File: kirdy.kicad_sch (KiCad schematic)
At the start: 10 parts, among them J1 Kirdy Front Panel, J12 Kirdy LD Adapter

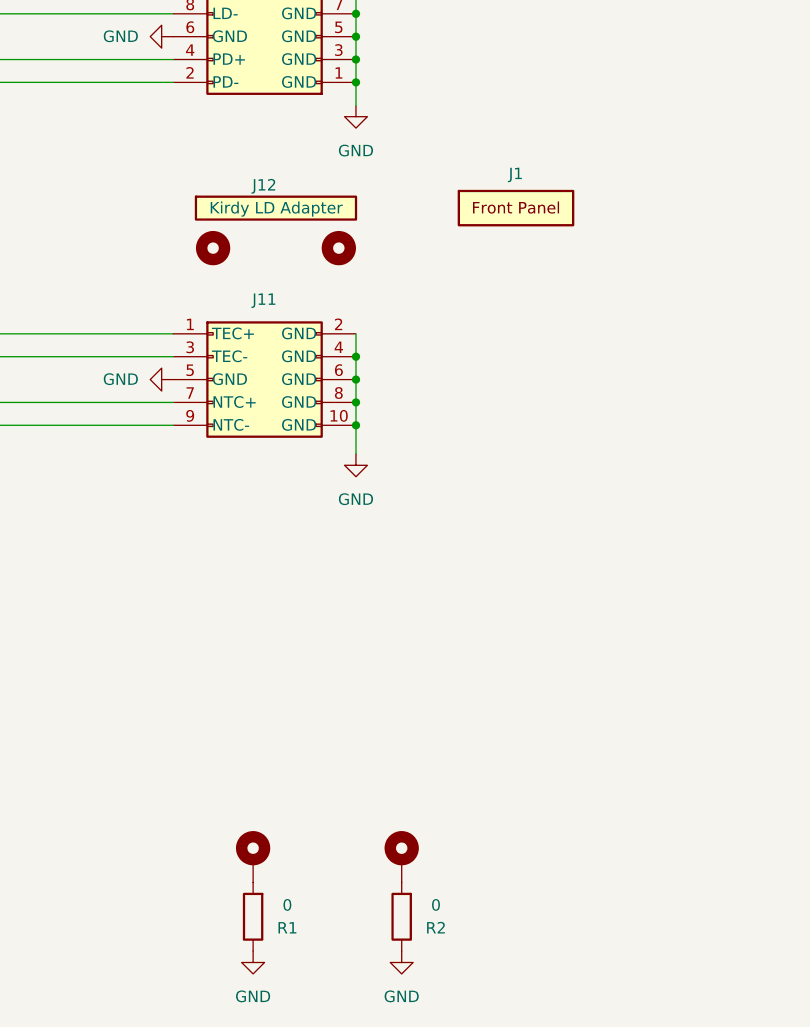
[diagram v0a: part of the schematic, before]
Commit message: sch, pcb:Edit PCB shape for connectors to protrude - Connectors now protrude the front panel - Align the connectors by the outline generated from 3D Model - Update the front panel symbol to include the two mounting holes
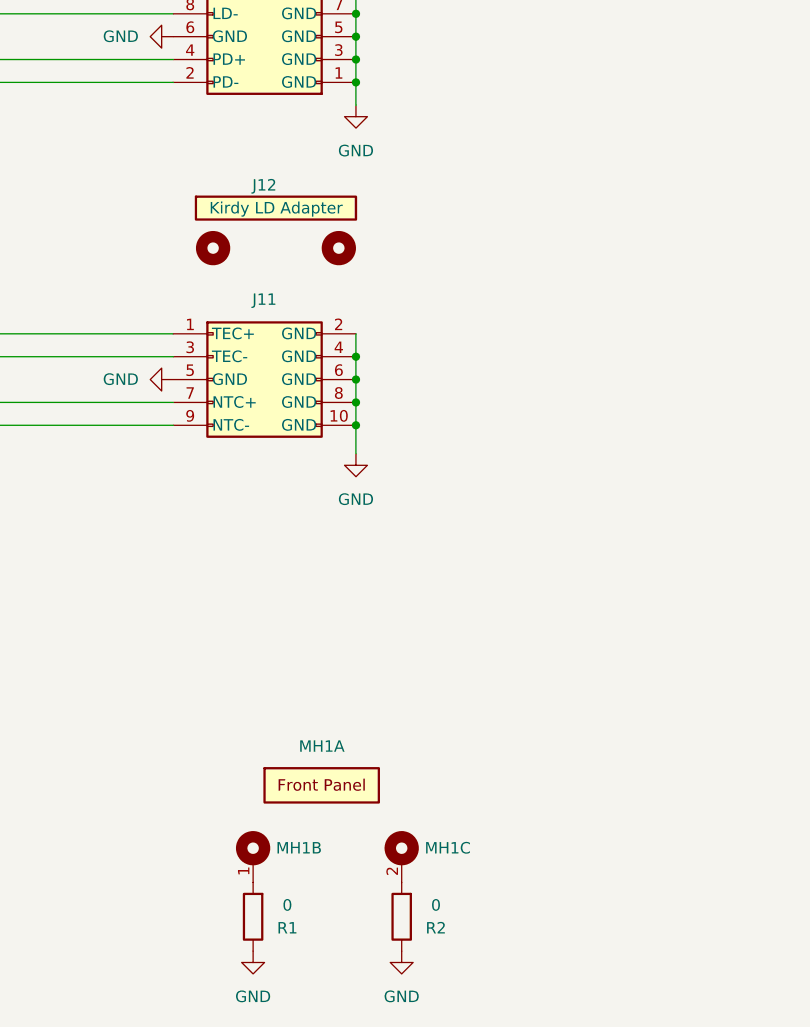
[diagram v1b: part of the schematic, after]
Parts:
- removed H1, H2: MountingHole_Pad, MountingHole:MountingHole_2.7mm_M2.5_Pad_Via, symbol Mechanical:MountingHole_Pad
- added unit 3 of MH1
- added unit 2 of MH1
- renumbered J1 to MH1
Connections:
- net at R1.2: now also MH1.1
- net at R2.2: now also MH1.2
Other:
- moved on the sheet: MH1A
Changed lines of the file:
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@@
+    )
+  )
+  (symbol (lib_id "kirdy:Panel") (at 309.88 208.28 270) (unit 3)
+    (in_bom yes) (on_board yes) (dnp no) (fields_autoplaced)
+    (property "Reference" "MH1" (at 312.42 208.28 90)
+      (effects (font (size 1.27 1.27)) (justify left))
+    )
+    (property "Value" "Kirdy Front Panel" (at 309.88 208.28 0)
+      (effects (font (size 1.27 1.27)) hide)
+    )
+    (property "Footprint" "kirdy:Panel" (at 309.88 208.28 0)
+      (effects (font (size 1.27 1.27)) hide)
+    )
+    (property "Datasheet" "" (at 309.88 208.28 0)
+      (effects (font (size 1.27 1.27)) hide)
+    )
+    (property "MFR_PN" "Kirdy Front Panel" (at 309.88 208.28 0)
+      (effects (font (size 1.27 1.27)) hide)
+    )
+    (pin "1")
+    (pin "2")
+    (instances
+      (project "kirdy"
+        (path "/88da1dd8-9274-4b55-84fb-90006c9b6e8f"
+          (reference "MH1") (unit 3)
+        )
+      )
     )
   )
@@
     )
   )
-  (symbol (lib_id "kirdy:Panel") (at 316.23 135.255 0) (unit 1)
-    (in_bom yes) (on_board yes) (dnp no) (fields_autoplaced)
-    (property "Reference" "J1" (at 322.58 133.35 0)
-      (effects (font (size 1.27 1.27)))
-    )
-    (property "Value" "Kirdy Front Panel" (at 316.23 135.255 0)
-      (effects (font (size 1.27 1.27)) hide)
-    )
-    (property "Footprint" "kirdy:Panel" (at 316.23 135.255 0)
-      (effects (font (size 1.27 1.27)) hide)
-    )
-    (property "Datasheet" "" (at 316.23 135.255 0)
-      (effects (font (size 1.27 1.27)) hide)
-    )
-    (property "MFR_PN" "Kirdy Front Panel" (at 322.58 133.35 0)
-      (effects (font (size 1.27 1.27)) hide)
-    )
-    (instances
-      (project "kirdy"
-        (path "/88da1dd8-9274-4b55-84fb-90006c9b6e8f"
-          (reference "J1") (unit 1)
+  (symbol (lib_name "Panel_1") (lib_id "kirdy:Panel") (at 294.64 199.39 0) (unit 1)
+    (in_bom yes) (on_board yes) (dnp no) (fields_autoplaced)
+    (property "Reference" "MH1" (at 300.99 196.977 0)
+      (effects (font (size 1.27 1.27)))
+    )
+    (property "Value" "Kirdy Front Panel" (at 294.64 199.39 0)
+      (effects (font (size 1.27 1.27)) hide)
+    )
+    (property "Footprint" "kirdy:Panel" (at 294.64 199.39 0)
+      (effects (font (size 1.27 1.27)) hide)
+    )
+    (property "Datasheet" "" (at 294.64 199.39 0)
+      (effects (font (size 1.27 1.27)) hide)
+    )
+    (property "MFR_PN" "Kirdy Front Panel" (at 300.99 197.485 0)
+      (effects (font (size 1.27 1.27)) hide)
+    )
+    (pin "1")
+    (pin "2")
+    (instances
+      (project "kirdy"
+        (path "/88da1dd8-9274-4b55-84fb-90006c9b6e8f"
+          (reference "MH1") (unit 1)
         )
       )
@@
     )
   )
-  (symbol (lib_id "Mechanical:MountingHole_Pad") (at 293.37 209.55 0) (unit 1)
-    (in_bom no) (on_board yes) (dnp no) (fields_autoplaced)
-    (property "Reference" "H1" (at 295.91 207.0099 0)
-      (effects (font (size 1.27 1.27)) (justify left) hide)
-    )
-    (property "Value" "MountingHole_Pad" (at 295.91 209.5499 0)
-      (effects (font (size 1.27 1.27)) (justify left) hide)
-    )
-    (property "Footprint" "MountingHole:MountingHole_2.7mm_M2.5_Pad_Via" (at 293.37 209.55 0)
-      (effects (font (size 1.27 1.27)) hide)
-    )
-    (property "Datasheet" "~" (at 293.37 209.55 0)
-      (effects (font (size 1.27 1.27)) hide)
-    )
-    (pin "1")
-    (instances
-      (project "kirdy"
-        (path "/88da1dd8-9274-4b55-84fb-90006c9b6e8f"
-          (reference "H1") (unit 1)
-        )
-      )
-    )
-  )
-  (symbol (lib_id "Mechanical:MountingHole_Pad") (at 309.88 209.55 0) (unit 1)
-    (in_bom no) (on_board yes) (dnp no) (fields_autoplaced)
-    (property "Reference" "H2" (at 312.42 207.0099 0)
-      (effects (font (size 1.27 1.27)) (justify left) hide)
-    )
-    (property "Value" "MountingHole_Pad" (at 312.42 209.5499 0)
-      (effects (font (size 1.27 1.27)) (justify left) hide)
-    )
-    (property "Footprint" "MountingHole:MountingHole_2.7mm_M2.5_Pad_Via" (at 309.88 209.55 0)
-      (effects (font (size 1.27 1.27)) hide)
-    )
-    (property "Datasheet" "~" (at 309.88 209.55 0)
-      (effects (font (size 1.27 1.27)) hide)
-    )
-    (pin "1")
-    (instances
-      (project "kirdy"
-        (path "/88da1dd8-9274-4b55-84fb-90006c9b6e8f"
-          (reference "H2") (unit 1)
-        )
-      )
-    )
-  )
   (symbol (lib_id "Mechanical:MountingHole") (at 288.925 141.605 0) (unit 1)
     (in_bom yes) (on_board yes) (dnp no) (fields_autoplaced)
@@
         )
       )
+    )
+  )
+  (symbol (lib_id "kirdy:Panel") (at 293.37 208.28 270) (unit 2)
+    (in_bom yes) (on_board yes) (dnp no) (fields_autoplaced)
+    (property "Reference" "MH1" (at 295.91 208.28 90)
+      (effects (font (size 1.27 1.27)) (justify left))
+    )
+    (property "Value" "Kirdy Front Panel" (at 293.37 208.28 0)
+      (effects (font (size 1.27 1.27)) hide)
+    )
+    (property "Footprint" "kirdy:Panel" (at 293.37 208.28 0)
+      (effects (font (size 1.27 1.27)) hide)
+    )
+    (property "Datasheet" "" (at 293.37 208.28 0)
+      (effects (font (size 1.27 1.27)) hide)
+    )
+    (property "MFR_PN" "Kirdy Front Panel" (at 293.37 208.28 0)
+      (effects (font (size 1.27 1.27)) hide)
+    )
+    (pin "1")
+    (pin "2")
+    (instances
+      (project "kirdy"
+        (path "/88da1dd8-9274-4b55-84fb-90006c9b6e8f"
+          (reference "MH1") (unit 2)
+        )
+      )

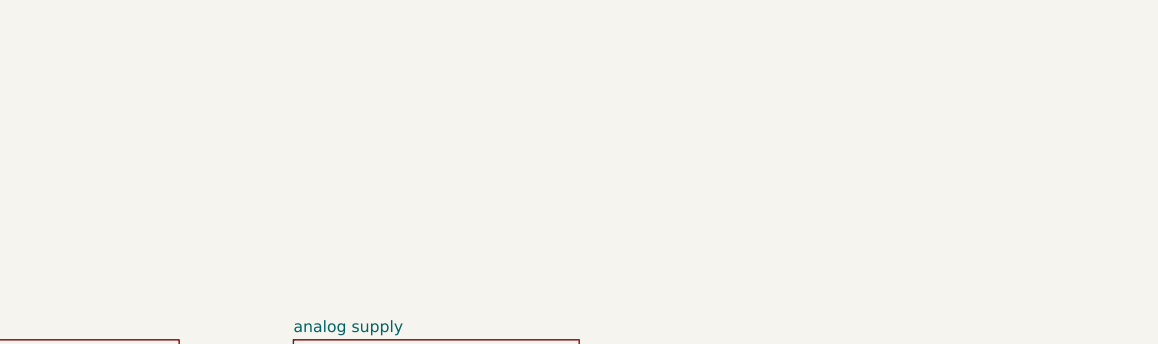
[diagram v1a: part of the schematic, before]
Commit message: sch, pcb: Remove X7R, X5R at input LT304x - Reduce the number of Tantalum Capacitor Used - Replace some non critical ones with Electrolytic Caps
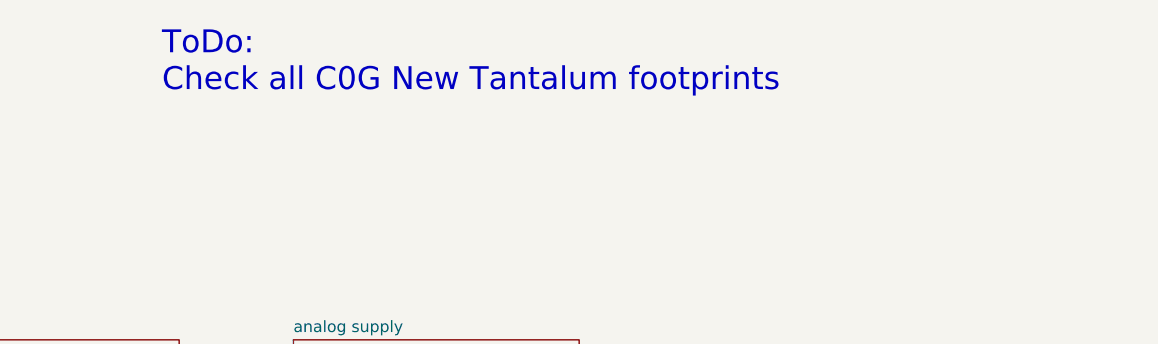
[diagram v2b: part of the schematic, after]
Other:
- note added: "ToDo: Check all C0G New Tantalum footprints"
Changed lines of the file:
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@@
     (stroke (width 0) (type default))
+  )
+  (text "ToDo:\nCheck all C0G New Tantalum footprints" (at 216.535 53.975 0)
+    (effects (font (size 2.54 2.54)) (justify left bottom))
   )
   (text "Possible Options:\nMating Height = 3.5mm(Header) + 5mm(Socket) = 8.5mm\n\nMale:  BG050-10A-0-0450-0737-0350-L-D <- need to use a custom footprint with positioning holes\nFemale: BG120-10-A-0-N-D <- need to use a custom footprint with positioning holes"

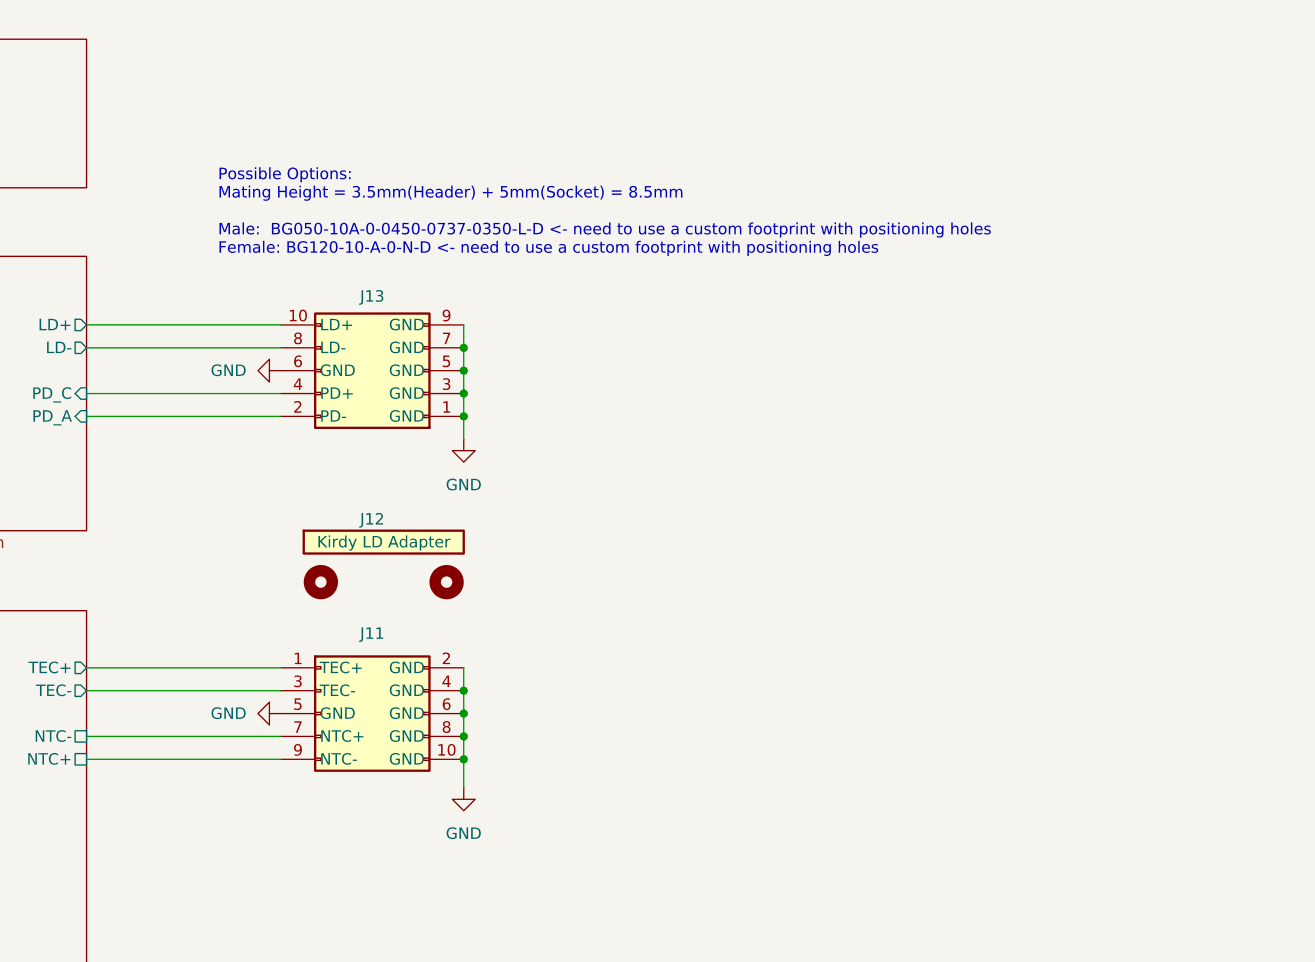
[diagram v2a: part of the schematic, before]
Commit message: sch, pcb: Change kirdy LD adpter connectors - Add two extra mounting holes for kirdy LD adapter - Update kirdy LD adapter 3D model - Update the PCB layout accordingly
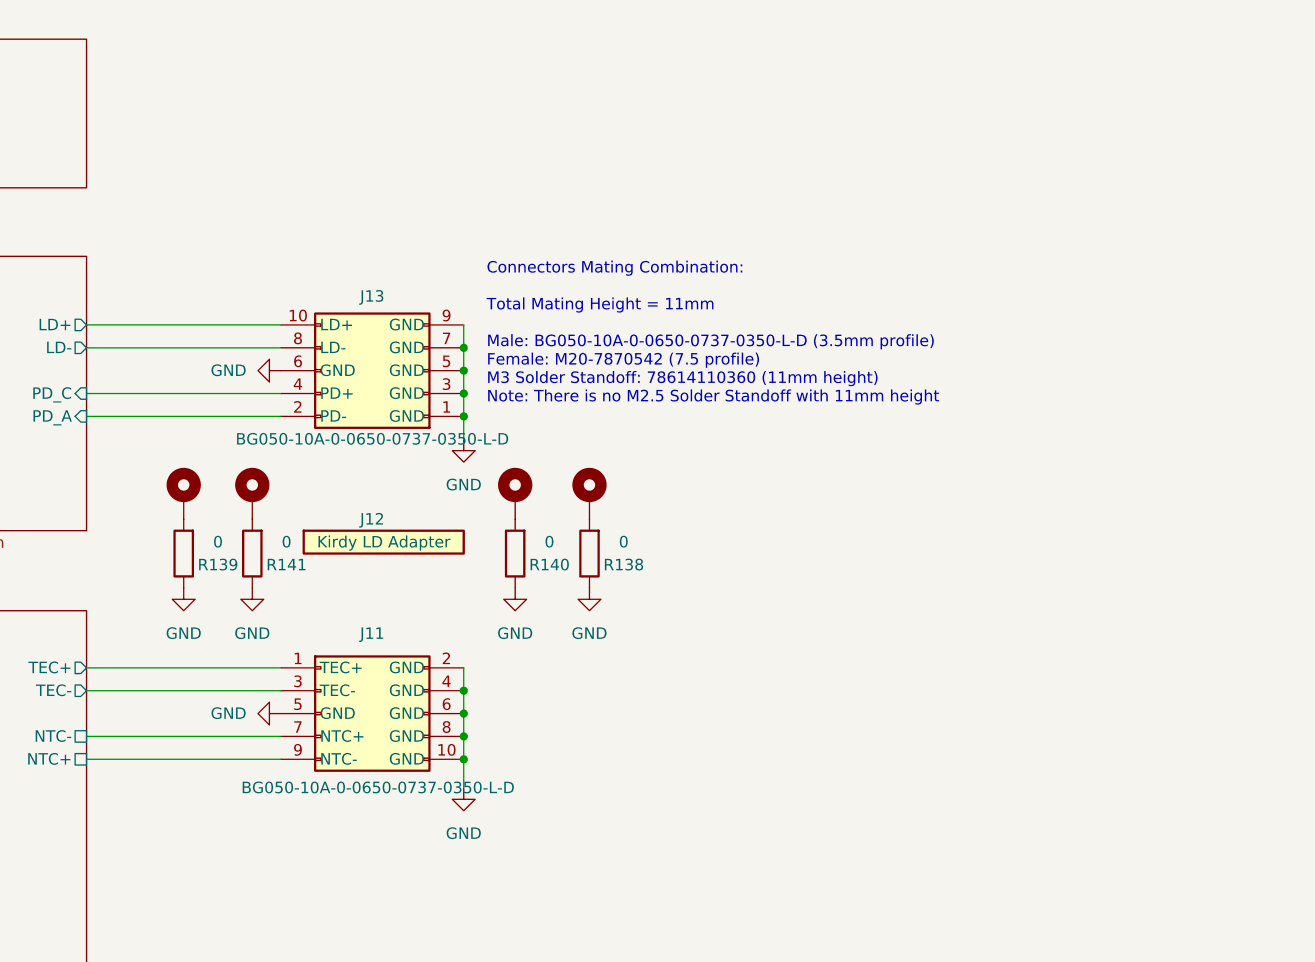
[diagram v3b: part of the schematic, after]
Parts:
- added H1, H2: 78614110360, Mounting_Wuerth:Mounting_Wuerth_WA-SMSI-M3_H11mm_9774110360, symbol Mechanical:MountingHole_Pad
- added R138, R139, R140, R141: 0, Resistor_SMD:R_0603_1608Metric, symbol Device:R
- H3: value MountingHole_Pad -> 78614110360; footprint MountingHole:MountingHole_2.7mm_M2.5 -> Mounting_Wuerth:Mounting_Wuerth_WA-SMSI-M3_H11mm_9774110360; symbol Mechanical:MountingHole -> Mechanical:MountingHole_Pad; MFR_PN (none) -> 78614110360; MFR_PN_ALT (none) -> 9774110360R
- H4: value MountingHole_Pad -> 78614110360; footprint MountingHole:MountingHole_2.7mm_M2.5 -> Mounting_Wuerth:Mounting_Wuerth_WA-SMSI-M3_H11mm_9774110360; symbol Mechanical:MountingHole -> Mechanical:MountingHole_Pad; MFR_PN (none) -> 78614110360; MFT_PN_ALT (none) -> 9774110360R
- J11, J13: value ~ -> BG050-10A-0-0650-0737-0350-L-D; footprint kirdy:BG050-10A-0-0450-0737-0350-L-D -> kirdy:BG050-10A-0-0650-0737-0350-L-D; MFR_PN (none) -> BG050-10A-0-0650-0737-0350-L-D
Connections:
- net GND: now also R138.1, R139.1, R140.1, R141.1
- new net: H3.1, R141.2
- new net: H4.1, R140.2
- new net: H1.1, R139.2
- new net: H2.1, R138.2
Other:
- note added: "Connectors Mating Combination: Total Mating Height = 11mm Male: BG050-10A-0-0650-0737-0350-L-D (3.5mm profile) Female: M20-7870542 (7.5 profile) M3 Solder Standoff: 78614110360 (11mm height) Note: There is no M2.5 Solder Standoff with 11mm height"
- note removed: "Possible Options: Mating Height = 3.5mm(Header) + 5mm(Socket) = 8.5mm Male: BG050-10A-0-0450-0737-0350-L-D <- need to use a custom footprint with positioning holes Female: BG120-10-A-0-N-D <- need to use a custom footprint with positioning holes"
